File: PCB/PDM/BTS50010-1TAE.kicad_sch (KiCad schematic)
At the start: 10 parts, among them IC3 BTS500101TAEATMA1

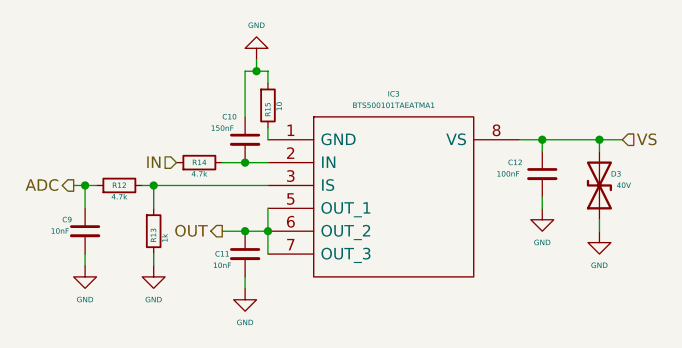
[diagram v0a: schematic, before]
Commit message: Added another high-side switch 2x7A + 2x4A SPI
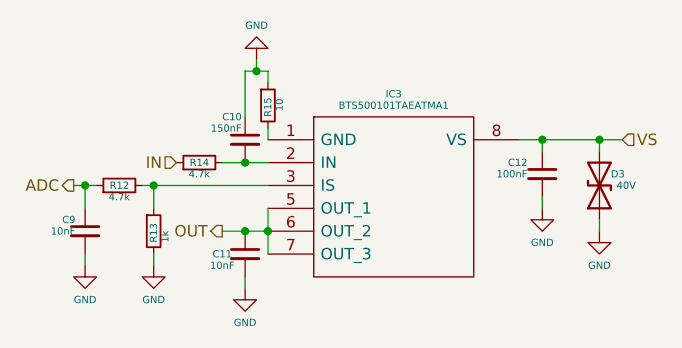
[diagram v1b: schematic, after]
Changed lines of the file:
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@@
     (in_bom yes) (on_board yes)
     (property "Reference" "C9" (id 0) (at 21.59 39.37 0)
-      (effects (font (size 0.6 0.6)) (justify left))
+      (effects (font (size 0.8 0.8)) (justify left))
     )
     (property "Value" "10nF" (id 1) (at 20.32 40.64 0)
-      (effects (font (size 0.6 0.6)) (justify left))
+      (effects (font (size 0.8 0.8)) (justify left))
     )
     (property "Footprint" "Capacitor_SMD:C_0402_1005Metric" (id 2) (at 24.13 40.64 0)
@@
     (in_bom yes) (on_board yes)
     (property "Reference" "#PWR0111" (id 0) (at 74.93 44.45 0)
-      (effects (font (size 0.6 0.6)) hide)
+      (effects (font (size 0.8 0.8)) hide)
     )
     (property "Value" "GND" (id 1) (at 74.93 41.91 0)
-      (effects (font (size 0.6 0.6)))
+      (effects (font (size 0.8 0.8)))
     )
     (property "Footprint" "" (id 2) (at 74.93 38.1 0)
@@
     (in_bom yes) (on_board yes)
     (property "Reference" "#PWR0112" (id 0) (at 81.28 46.99 0)
-      (effects (font (size 0.6 0.6)) hide)
+      (effects (font (size 0.8 0.8)) hide)
     )
     (property "Value" "GND" (id 1) (at 81.28 44.45 0)
-      (effects (font (size 0.6 0.6)))
+      (effects (font (size 0.8 0.8)))
     )
     (property "Footprint" "" (id 2) (at 81.28 40.64 0)
@@
     (in_bom yes) (on_board yes)
     (property "Reference" "IC3" (id 0) (at 58.42 25.4 0)
-      (effects (font (size 0.6 0.6)))
+      (effects (font (size 0.8 0.8)))
     )
     (property "Value" "BTS500101TAEATMA1" (id 1) (at 58.42 26.67 0)
-      (effects (font (size 0.6 0.6)))
+      (effects (font (size 0.8 0.8)))
     )
     (property "Footprint" "PDM_Additional:PG-TO263-7-3_3" (id 2) (at 68.58 27.94 0)
@@
     (in_bom yes) (on_board yes)
     (property "Reference" "R12" (id 0) (at 27.94 35.56 90)
-      (effects (font (size 0.6 0.6)))
+      (effects (font (size 0.8 0.8)))
     )
     (property "Value" "4.7k" (id 1) (at 27.94 36.83 90)
-      (effects (font (size 0.6 0.6)))
+      (effects (font (size 0.8 0.8)))
     )
     (property "Footprint" "Resistor_SMD:R_0402_1005Metric" (id 2) (at 27.94 35.56 0)
@@
     (in_bom yes) (on_board yes)
     (property "Reference" "#PWR0113" (id 0) (at 43.18 15.24 0)
-      (effects (font (size 0.6 0.6)) hide)
+      (effects (font (size 0.8 0.8)) hide)
     )
     (property "Value" "GND" (id 1) (at 43.18 17.78 0)
-      (effects (font (size 0.6 0.6)))
+      (effects (font (size 0.8 0.8)))
     )
     (property "Footprint" "" (id 2) (at 43.18 21.59 0)
@@
     (in_bom yes) (on_board yes)
     (property "Reference" "R15" (id 0) (at 44.45 27.94 90)
-      (effects (font (size 0.6 0.6)) (justify left))
+      (effects (font (size 0.8 0.8)) (justify left))
     )
     (property "Value" "10" (id 1) (at 45.72 27.305 90)
-      (effects (font (size 0.6 0.6)) (justify left))
+      (effects (font (size 0.8 0.8)) (justify left))
     )
     (property "Footprint" "Resistor_SMD:R_0402_1005Metric" (id 2) (at 44.45 26.67 0)
@@
     (in_bom yes) (on_board yes)
     (property "Reference" "#PWR0110" (id 0) (at 31.75 50.8 0)
-      (effects (font (size 0.6 0.6)) hide)
+      (effects (font (size 0.8 0.8)) hide)
     )
     (property "Value" "GND" (id 1) (at 31.75 48.26 0)
-      (effects (font (size 0.6 0.6)))
+      (effects (font (size 0.8 0.8)))
     )
     (property "Footprint" "" (id 2) (at 31.75 44.45 0)
@@
     (in_bom yes) (on_board yes)
     (property "Reference" "C12" (id 0) (at 71.12 33.02 0)
-      (effects (font (size 0.6 0.6)) (justify left))
+      (effects (font (size 0.8 0.8)) (justify left))
     )
     (property "Value" "100nF" (id 1) (at 69.85 34.29 0)
-      (effects (font (size 0.6 0.6)) (justify left))
+      (effects (font (size 0.8 0.8)) (justify left))
     )
     (property "Footprint" "Capacitor_SMD:C_0805_2012Metric" (id 2) (at 74.93 34.29 0)
@@
     (in_bom yes) (on_board yes)
     (property "Reference" "#PWR0109" (id 0) (at 24.13 50.8 0)
-      (effects (font (size 0.6 0.6)) hide)
+      (effects (font (size 0.8 0.8)) hide)
     )
     (property "Value" "GND" (id 1) (at 24.13 48.26 0)
-      (effects (font (size 0.6 0.6)))
+      (effects (font (size 0.8 0.8)))
     )
     (property "Footprint" "" (id 2) (at 24.13 44.45 0)
@@
     (in_bom yes) (on_board yes)
     (property "Reference" "C11" (id 0) (at 39.37 43.18 0)
-      (effects (font (size 0.6 0.6)))
+      (effects (font (size 0.8 0.8)))
     )
     (property "Value" "10nF" (id 1) (at 39.37 44.45 0)
-      (effects (font (size 0.6 0.6)))
+      (effects (font (size 0.8 0.8)))
     )
     (property "Footprint" "Capacitor_SMD:C_0402_1005Metric" (id 2) (at 41.91 43.18 0)
@@
     (in_bom yes) (on_board yes)
     (property "Reference" "D3" (id 0) (at 82.55 34.29 90)
-      (effects (font (size 0.6 0.6)) (justify right))
+      (effects (font (size 0.8 0.8)) (justify right))
     )
     (property "Value" "40V" (id 1) (at 83.185 35.56 90)
-      (effects (font (size 0.6 0.6)) (justify right))
+      (effects (font (size 0.8 0.8)) (justify right))
     )
     (property "Footprint" "Diode_SMD:D_0805_2012Metric" (id 2) (at 81.28 35.56 0)
@@
     (in_bom yes) (on_board yes)
     (property "Reference" "C10" (id 0) (at 39.37 27.94 0)
-      (effects (font (size 0.6 0.6)) (justify left))
+      (effects (font (size 0.8 0.8)) (justify left))
     )
     (property "Value" "150nF" (id 1) (at 38.1 29.21 0)
-      (effects (font (size 0.6 0.6)) (justify left))
+      (effects (font (size 0.8 0.8)) (justify left))
     )
     (property "Footprint" "Capacitor_SMD:C_0805_2012Metric" (id 2) (at 41.91 30.48 0)
@@
     (in_bom yes) (on_board yes)
     (property "Reference" "R14" (id 0) (at 36.83 33.02 90)
-      (effects (font (size 0.6 0.6)))
+      (effects (font (size 0.8 0.8)))
     )
     (property "Value" "4.7k" (id 1) (at 36.83 34.29 90)
-      (effects (font (size 0.6 0.6)))
+      (effects (font (size 0.8 0.8)))
     )
     (property "Footprint" "Resistor_SMD:R_0402_1005Metric" (id 2) (at 36.83 33.02 0)
@@
     (in_bom yes) (on_board yes)
     (property "Reference" "#PWR0108" (id 0) (at 41.91 53.34 0)
-      (effects (font (size 0.6 0.6)) hide)
+      (effects (font (size 0.8 0.8)) hide)
     )
     (property "Value" "GND" (id 1) (at 41.91 50.8 0)
-      (effects (font (size 0.6 0.6)))
+      (effects (font (size 0.8 0.8)))
     )
     (property "Footprint" "" (id 2) (at 41.91 46.99 0)
@@
     (in_bom yes) (on_board yes)
     (property "Reference" "R13" (id 0) (at 31.75 41.91 90)
-      (effects (font (size 0.6 0.6)) (justify left))
+      (effects (font (size 0.8 0.8)) (justify left))
     )
     (property "Value" "1k" (id 1) (at 33.02 41.91 90)
-      (effects (font (size 0.6 0.6)) (justify left))
+      (effects (font (size 0.8 0.8)) (justify left))
     )
     (property "Footprint" "Resistor_SMD:R_0402_1005Metric" (id 2) (at 31.75 40.64 0)
